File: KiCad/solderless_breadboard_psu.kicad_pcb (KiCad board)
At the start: 4 copper layers, 55 x 51 mm, 87 parts, among them IC301 MCP73831T-2ACI_OT, IC302 BQ29737DSER, IC401 TLV62569DBVR, IC501 FT232RL-REEL, J201 Barrel_Jack_Switch_Pin3Ring, J301 BM02B-GHS-TBT_LF__SN__N_, J501 Conn_01x09_Pin, J502 Conn_01x09_Pin, J503 Conn_01x06_Pin, J504 USB_C_Receptacle_USB2.0_16P, J601 Conn_02x03_Odd_Even, J602 Conn_02x03_Odd_Even, Q301 DMG3415U-7, Q302 T2N7002AK, Q303 T2N7002AK, U401 TPS61040DBVR, U501 USBLC6-2SC6

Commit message: battery connector update
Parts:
- D401: footprint Diode_SMD:D_SMA -> Diode_SMD:D_0603_1608Metric
- J301: value BM02B-GHS-TBT_LF__SN__N_ -> Conn_01x02; footprint psu:BM02B-GHS-TBT_1 -> Connector_PinHeader_2.54mm:PinHeader_1x02_P2.54mm_Vertical
- moved J301 2.32 mm to (26.0, 87.7), turned to 0 degrees
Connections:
- J301 pad 1: CELL- -> CELL+
- J301 pad 2: CELL+ -> CELL-
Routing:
- net CELL+: track 9.71 -> 13.3 mm
- net CELL-: track 7.73 -> 9.99 mm
- net GND: vias 148 -> 150

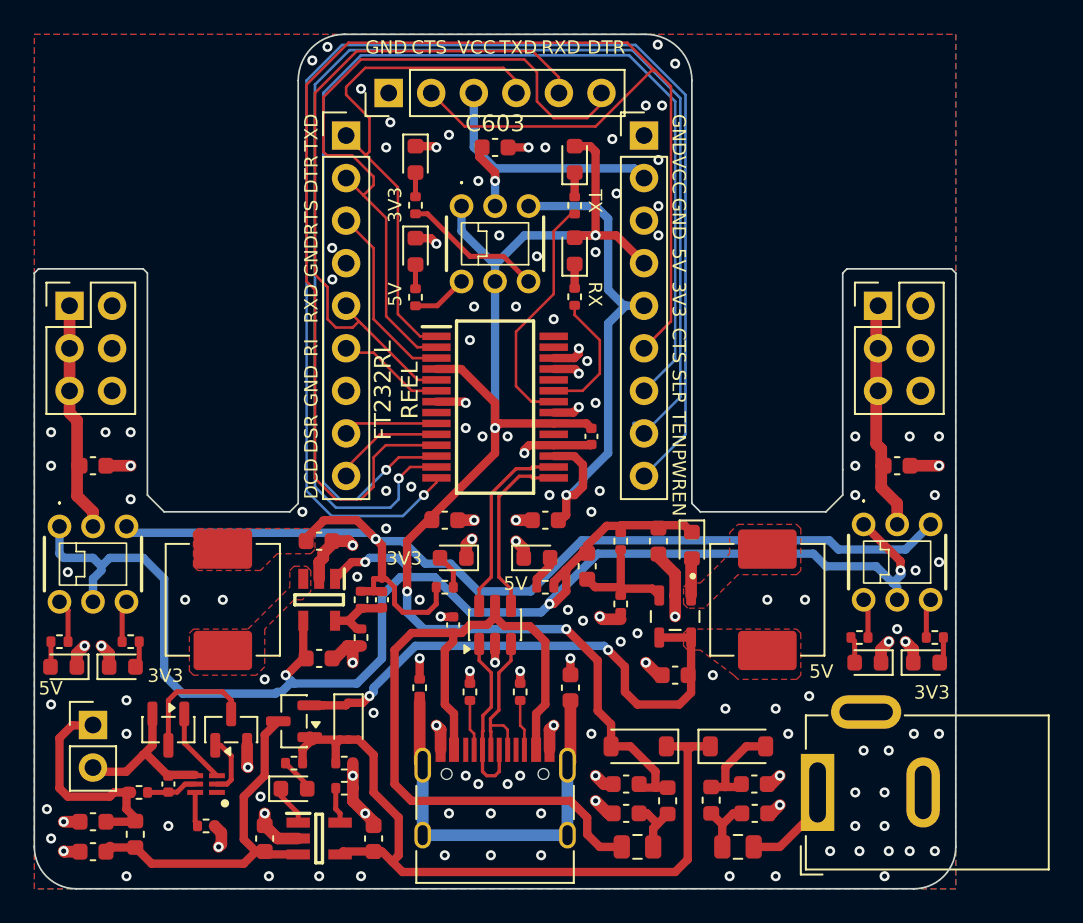
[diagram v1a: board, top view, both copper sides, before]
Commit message: Update battery connector
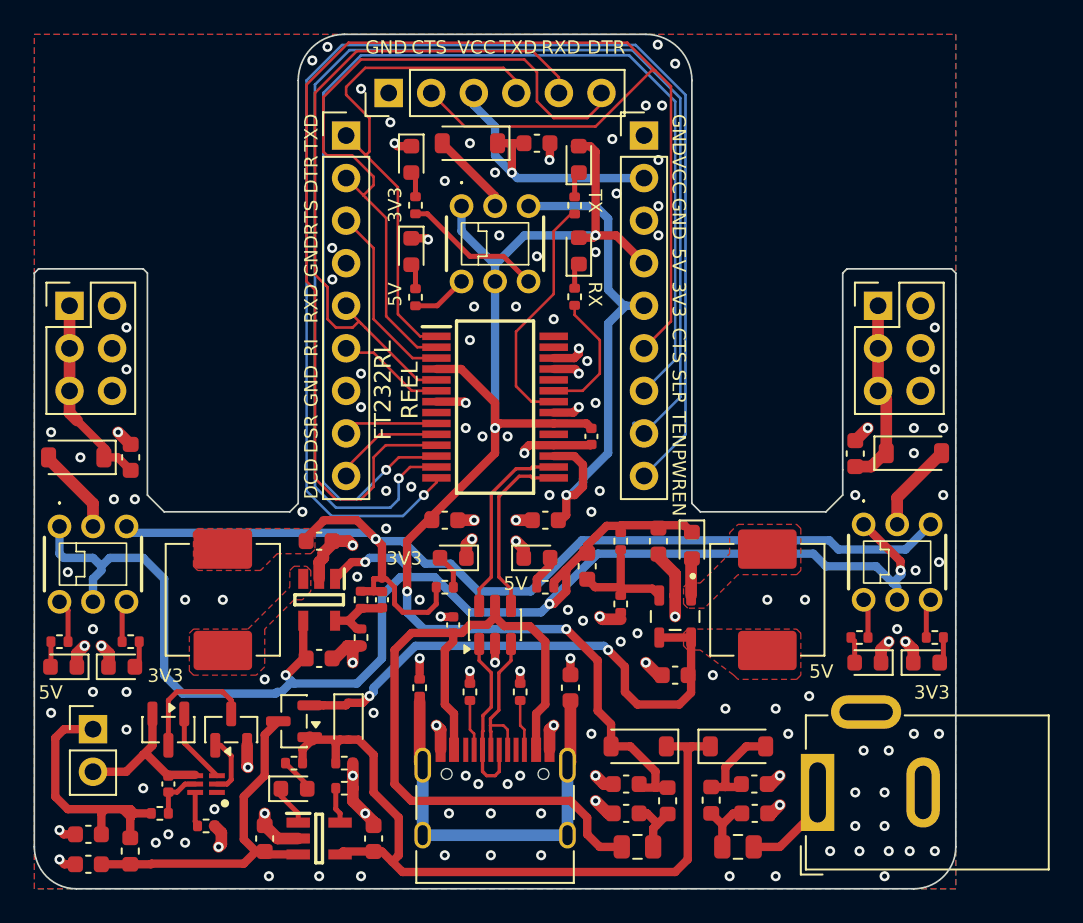
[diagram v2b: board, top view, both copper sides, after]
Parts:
- added D607: 1N5819HW-7-F, Diode_SMD:D_SOD-123, F.Cu at (48.5, 53.0)
- added D608: LED, LED_SMD:LED_0603_1608Metric, F.Cu at (45.0, 59.5)
- added D609: LED, LED_SMD:LED_0603_1608Metric, F.Cu at (45.0, 54.0)
- D602, D605: value LED -> 1N5819HW-7-F; footprint LED_SMD:LED_0603_1608Metric -> Diode_SMD:D_SOD-123
- moved D603 44.5 mm to (27.7, 84.2), turned to 0 degrees
- moved D606 42.8 mm to (75.8, 84.0), turned to 0 degrees
- moved D605 32.1 mm to (75.0, 71.5), turned to 0 degrees
- moved D602 12.8 mm to (25.0, 71.8), turned to 180 degrees
- moved D604 3.50 mm to (72.2, 84.0), turned to 180 degrees
- moved C602 2.60 mm to (71.5, 71.5), turned to 90 degrees
- moved C603 2.51 mm to (52.5, 53.0)
- moved C601 2.30 mm to (28.2, 71.8), turned to 90 degrees
- moved R304 1.76 mm to (30.0, 93.0)
- moved FB301 1.04 mm to (28.2, 95.2)
- moved C303 0.80 mm to (25.7, 94.2)
- moved C304 0.80 mm to (25.7, 96.0)
- moved D501 0.25 mm to (55.0, 59.4)
- moved D502 0.25 mm to (55.0, 54.0)
- moved J301 0.25 mm to (26.0, 88.0)
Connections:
- D602 pad 1: GND -> VCC_L
- D605 pad 1: GND -> VCC_R
- R602 pad 1: Net-(D602-A) -> Net-(D603-A)
- R603 pad 1: Net-(D603-A) -> Net-(D604-A)
- R604 pad 1: Net-(D604-A) -> Net-(D606-A)
- R605 pad 1: Net-(D605-A) -> Net-(D608-A)
- R606 pad 1: Net-(D606-A) -> Net-(D609-A)
- S601 pad 2: VCC_L -> Net-(D602-A)
- S602 pad 2: VCC_R -> Net-(D605-A)
- S603 pad 2: VCC_FTDI -> Net-(D607-A)
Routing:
- net Net-(D607-A): track 0.00 -> 5.05 mm
- net Net-(D605-A): track 1.44 -> 5.35 mm
- net Net-(D602-A): track 1.59 -> 5.22 mm
- net CELL+: track 13.3 -> 15.6 mm
- net VCC_R: track 13.6 -> 11.3 mm
- net VCC_L: track 13.8 -> 11.9 mm
- net VCC_FTDI: track 18.8 -> 17.0 mm
- net Net-(D609-A): track 0.00 -> 1.55 mm
- net Net-(D608-A): track 0.00 -> 1.54 mm
- net GND: track 65.8 -> 64.6 mm, vias 150 -> 155

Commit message: Update pin header offset. Clean DRC error
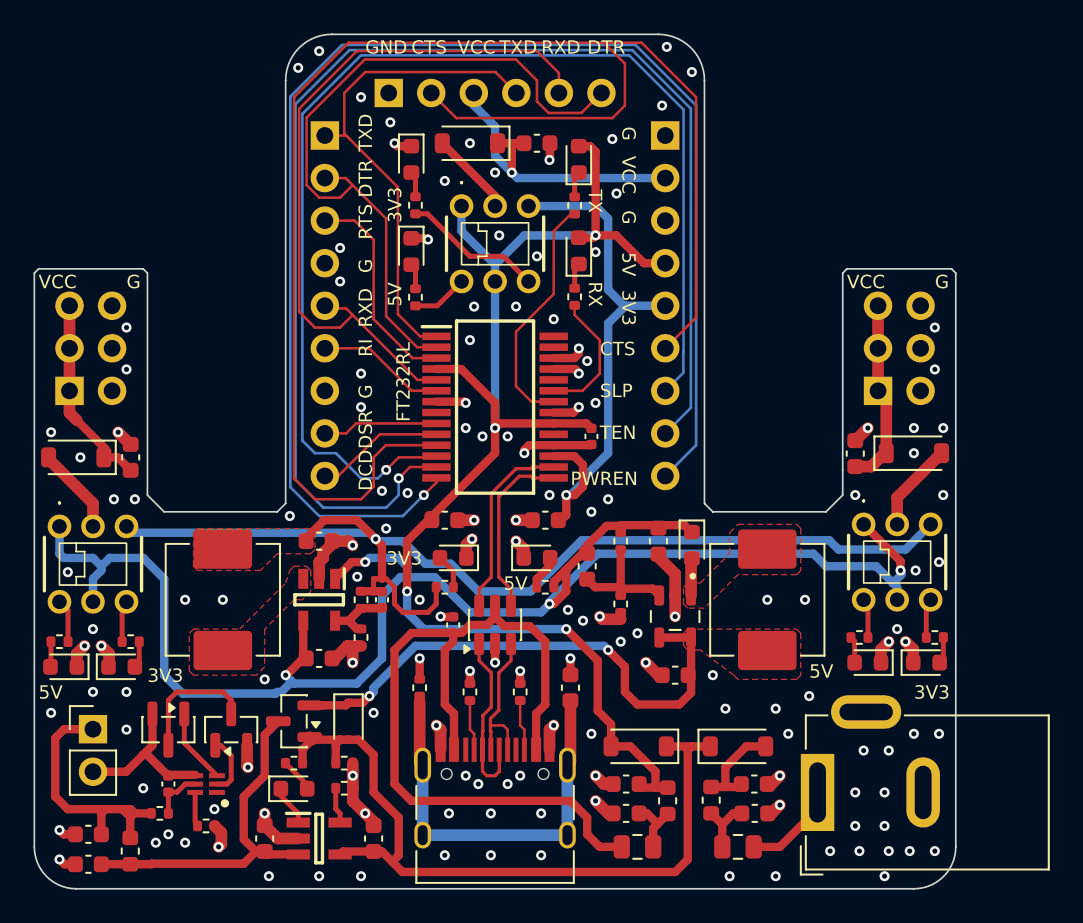
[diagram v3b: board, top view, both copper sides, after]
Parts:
- J501, J502, J503, J601, J602: moved to B.Cu
- moved J601 5.08 mm to (24.6, 67.8)
- moved J602 5.08 mm to (72.9, 67.8)
- moved J501 1.27 mm to (60.2, 52.5), turned to 180 degrees
- moved J502 1.27 mm to (39.8, 52.5), turned to 180 degrees
- turned J503 to -90 degrees
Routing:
- net /[5]USB 2 UART/CTS: track 89.6 -> 93.3 mm
- net /[5]USB 2 UART/RXD: track 40.7 -> 43.2 mm
- net /[5]USB 2 UART/DTR: track 42.2 -> 43.9 mm
- net /[5]USB 2 UART/RTS: track 11.3 -> 12.8 mm
- net VCC_FTDI: track 17.0 -> 18.3 mm
- net /[5]USB 2 UART/DSR: track 5.64 -> 6.91 mm
- net +VCC_USB2UART_FILT: track 81.2 -> 82.5 mm
- net +3V3_FTDI: track 30.9 -> 32.1 mm
- net /[5]USB 2 UART/RI: track 6.44 -> 7.71 mm
- net /[5]USB 2 UART/PWREN: track 82.5 -> 83.7 mm
- net /[5]USB 2 UART/TXD: track 31.3 -> 30.0 mm
- net /[5]USB 2 UART/DCD: track 6.69 -> 7.69 mm
- net /[5]USB 2 UART/SLEEP: track 72.6 -> 71.8 mm
- net GND: vias 155 -> 151
- removed copper zone on B.Cu, net GND
- removed copper zone on F.Cu, net GND
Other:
- outline, holes or cut-outs redrawn
- board text added: "FT232RL"
- board text added: "G"
- board text removed: "FT232RL REEL"

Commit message: JLCPCB check fixes
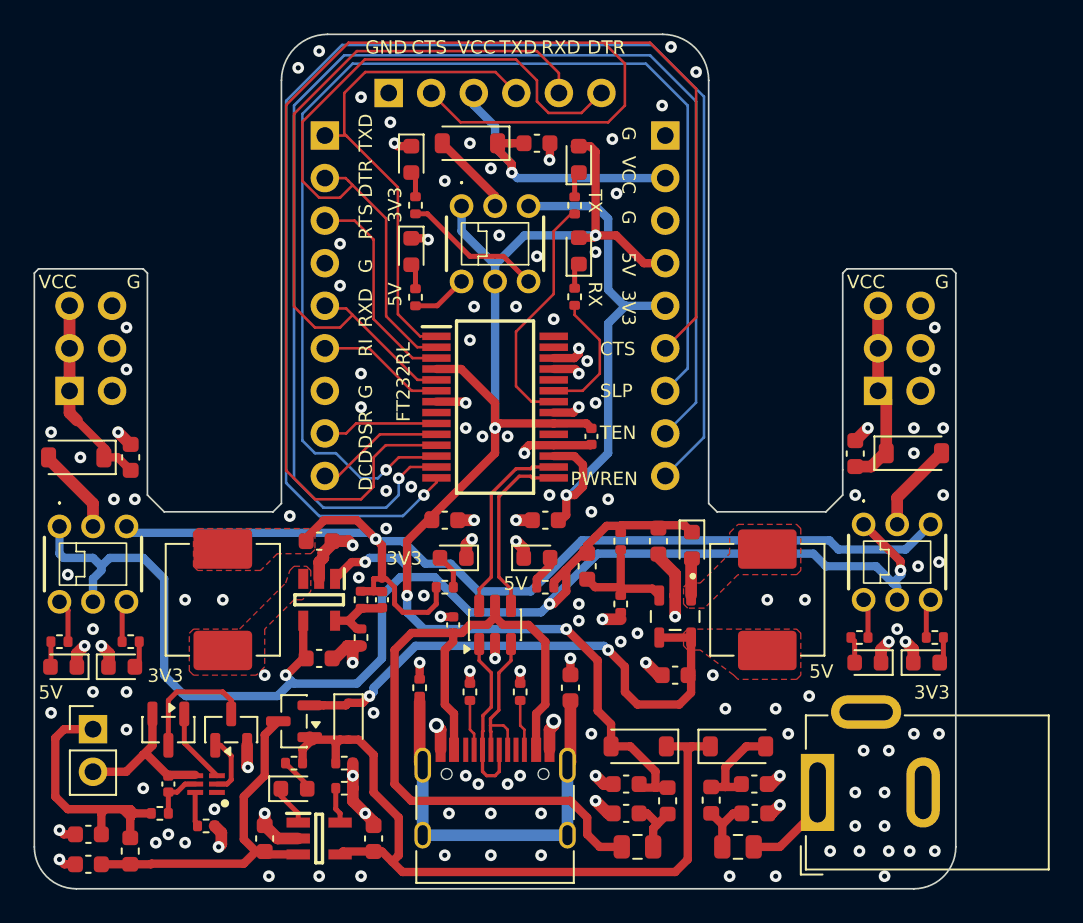
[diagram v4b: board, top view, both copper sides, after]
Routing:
- net /[5]USB 2 UART/PWREN: track 83.7 -> 84.9 mm
- net /[5]USB 2 UART/CTS: track 93.3 -> 94.2 mm
- net /[5]USB 2 UART/TEN: track 79.5 -> 80.0 mm
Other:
- outline, holes or cut-outs redrawn

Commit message: Update resistor values
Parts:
- R402, R505: value 1MR -> 910kR
- R404: value 330kR -> 300kR
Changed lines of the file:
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@@
 			(at 0 1.43 270)
 			(layer "F.Fab")
+			(hide yes)
 			(effects
 				(font
@@
 			)
 		)
-		(property "Manufacturer" "UNI-ROYAL(Uniroyal Elec)"
+		(property "Manufacturer" "UNI-ROYAL"
 			(at 0 0 90)
 			(unlocked yes)
@@
 			)
 		)
-		(property "Manufacturer" "UNI-ROYAL(Uniroyal Elec)"
+		(property "Manufacturer" "UNI-ROYAL"
 			(at 0 0 0)
 			(unlocked yes)
@@
 			)
 		)
-		(property "Manufacturer" "UNI-ROYAL(Uniroyal Elec)"
+		(property "Manufacturer" "UNI-ROYAL"
 			(at 0 0 90)
 			(unlocked yes)
@@
 			)
 		)
-		(property "Value" "1MR"
+		(property "Value" "910kR"
 			(at 0 1.17 90)
 			(layer "F.Fab")
+			(hide yes)
 			(effects
 				(font
@@
 			)
 		)
-		(property "Manufacturer" "UNI-ROYAL(Uniroyal Elec)"
+		(property "Manufacturer" "UNI-ROYAL"
 			(at 0 0 90)
 			(unlocked yes)
@@
 			)
 		)
-		(property "Manufacturer Part Number" "0402WGF1004TCE"
+		(property "Manufacturer Part Number" "0402WGJ0914TCE"
 			(at 0 0 90)
 			(unlocked yes)
@@
 			)
 		)
-		(property "Manufacturer" "UNI-ROYAL(Uniroyal Elec)"
+		(property "Manufacturer" "UNI-ROYAL"
 			(at 0 0 180)
 			(unlocked yes)
@@
 			)
 		)
-		(property "Manufacturer" "UNI-ROYAL(Uniroyal Elec)"
+		(property "Manufacturer" "UNI-ROYAL"
 			(at 0 0 0)
 			(unlocked yes)
@@
 			)
 		)
-		(property "Manufacturer" "UNI-ROYAL(Uniroyal Elec)"
+		(property "Manufacturer" "UNI-ROYAL"
 			(at 0 0 180)
 			(unlocked yes)
@@
 			)
 		)
+		(property ki_fp_filters "LED* LED_SMD:* LED_THT:*")
+		(sheetname "/[6]Power out/")
+		(sheetfile "06_power_out.kicad_sch")
 		(attr smd)
 		(fp_line
@@
 			)
 		)
-		(property "Manufacturer" "STMicroelectronics"
+		(property "Manufacturer" "ST"
 			(at 0 0 90)
 			(unlocked yes)
@@
 			)
 		)
+		(property ki_fp_filters "LED* LED_SMD:* LED_THT:*")
+		(sheetname "/[6]Power out/")
+		(sheetfile "06_power_out.kicad_sch")
 		(attr smd)
 		(fp_line
@@
 			(at 0 1.43 180)
 			(layer "F.Fab")
+			(hide yes)
 			(effects
 				(font
@@
 			)
 		)
-		(property "Manufacturer" "UNI-ROYAL(Uniroyal Elec)"
+		(property "Manufacturer" "UNI-ROYAL"
 			(at 0 0 90)
 			(unlocked yes)
@@
 			)
 		)
-		(property "Manufacturer" "cjiang (Changjiang Microelectronics Tech)"
+		(property "Manufacturer" "cjiang"
 			(at 0 0 90)
 			(unlocked yes)
@@
 			)
 		)
-		(property "Value" "1MR"
+		(property "Value" "910kR"
 			(at 0 1.17 270)
 			(layer "F.Fab")
+			(hide yes)
 			(effects
 				(font
@@
 			)
 		)
-		(property "Manufacturer" "UNI-ROYAL(Uniroyal Elec)"
+		(property "Manufacturer" "UNI-ROYAL"
 			(at 0 0 270)
 			(unlocked yes)
@@
 			)
 		)
-		(property "Manufacturer Part Number" "0402WGF1004TCE"
+		(property "Manufacturer Part Number" "0402WGJ0914TCE"
 			(at 0 0 270)
 			(unlocked yes)
@@
 			)
 		)
-		(property "Manufacturer" "UNI-ROYAL(Uniroyal Elec)"
+		(property "Manufacturer" "UNI-ROYAL"
 			(at 0 0 0)
 			(unlocked yes)
@@
 			)
 		)
-		(property "Value" "330kR"
+		(property "Value" "300kR"
 			(at 0 1.17 270)
 			(layer "F.Fab")
+			(hide yes)
 			(effects
 				(font
@@
 			)
 		)
-		(property "Manufacturer" "UNI-ROYAL(Uniroyal Elec)"
+		(property "Manufacturer" "UNI-ROYAL"
 			(at 0 0 270)
 			(unlocked yes)
@@
 			)
 		)
-		(property "Manufacturer Part Number" "0402WGF3303TCE"
+		(property "Manufacturer Part Number" "0402WGF3003TCE"
 			(at 0 0 270)
 			(unlocked yes)
@@
 			)
 		)
-		(property "Manufacturer" "UNI-ROYAL(Uniroyal Elec)"
+		(property "Manufacturer" "UNI-ROYAL"
 			(at 0 0 0)
 			(unlocked yes)
@@
 			)
 		)
-		(property "Manufacturer" "UNI-ROYAL(Uniroyal Elec)"
+		(property "Manufacturer" "UNI-ROYAL"
 			(at 0 0 270)
 			(unlocked yes)
@@
 			)
 		)
-		(property "Manufacturer" "UNI-ROYAL(Uniroyal Elec)"
+		(property "Manufacturer" "UNI-ROYAL"
 			(at 0 0 90)
 			(unlocked yes)
@@
 			)
 		)
-		(property "Manufacturer" "UNI-ROYAL(Uniroyal Elec)"
+		(property "Manufacturer" "UNI-ROYAL"
 			(at 0 0 0)
 			(unlocked yes)
@@
 			)
 		)
-		(property "Manufacturer" "UNI-ROYAL(Uniroyal Elec)"
+		(property "Manufacturer" "UNI-ROYAL"
 			(at 0 0 0)
 			(unlocked yes)
@@
 			)
 		)
-		(property "Manufacturer" "Schottky Diode"
+		(property "Manufacturer" "Kyocera AVX"
 			(at 0 0 270)
 			(unlocked yes)
@@
 			)
 		)
-		(property "Manufacturer" "UNI-ROYAL(Uniroyal Elec)"
+		(property "Manufacturer" "UNI-ROYAL"
 			(at 0 0 0)
 			(unlocked yes)
@@
 			)
 		)
-		(property "Manufacturer" "UNI-ROYAL(Uniroyal Elec)"
+		(property "Manufacturer" "UNI-ROYAL"
 			(at 0 0 180)
 			(unlocked yes)
@@
 			)
 		)
-		(property "Manufacturer" "UNI-ROYAL(Uniroyal Elec)"
+		(property "Manufacturer" "UNI-ROYAL"
 			(at 0 0 180)
 			(unlocked yes)
@@
 			)
 		)
-		(property "Manufacturer" "UNI-ROYAL(Uniroyal Elec)"
+		(property "Manufacturer" "UNI-ROYAL"
 			(at 0 0 270)
 			(unlocked yes)
@@
 			)
 		)
-		(property "Manufacturer" "cjiang (Changjiang Microelectronics Tech)"
+		(property "Manufacturer" "cjiang"
 			(at 0 0 90)
 			(unlocked yes)
@@
 			(at 0 1.43 0)
 			(layer "F.Fab")
+			(hide yes)
 			(effects
 				(font
@@
 			)
 		)
-		(property "Manufacturer" "UNI-ROYAL(Uniroyal Elec)"
+		(property "Manufacturer" "UNI-ROYAL"
 			(at 0 0 90)
 			(unlocked yes)
@@
 			)
 		)
-		(property "Manufacturer" "UNI-ROYAL(Uniroyal Elec)"
+		(property "Manufacturer" "UNI-ROYAL"
 			(at 0 0 90)
 			(unlocked yes)
